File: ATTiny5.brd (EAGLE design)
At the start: 30 x 15 mm, 20 parts, among them Q1 BSP100, U1 SPX5205M5-L-3-3, U2 ATTINY5-TSHR, X1 DIODES, X2 INPUT

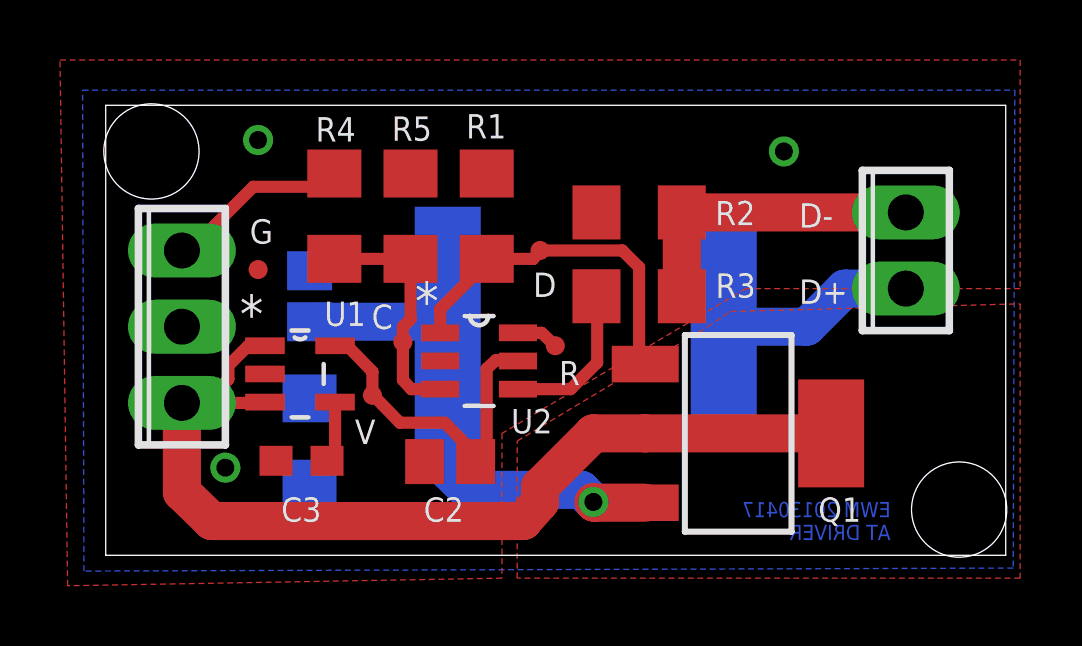
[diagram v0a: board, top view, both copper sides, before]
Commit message: Updated Board
Updated Board with Optional current limiting transistor and properly
sized and connected output cap.
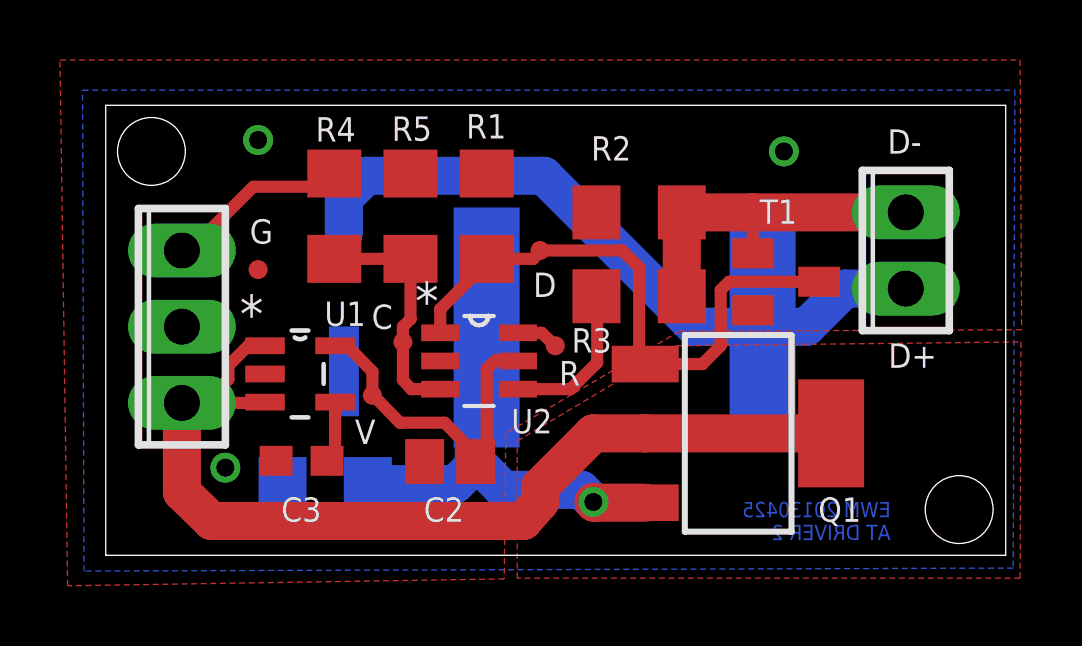
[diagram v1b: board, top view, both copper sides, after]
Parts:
- added T1: BC846, transistor:SOT23
- C1: value .1u -> 100u; device resistor:C0805 -> Personal:CDE-AVE-X
- moved D1 1.53 mm to (7.32, 2.37), turned to 0 degrees
- moved L1 1.30 mm to (17.3, 7.59)
- moved C1 1.16 mm to (7.94, 8.43)
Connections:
- net D-: now also T1.1
- net GND: now also C1.C-, T1.2; no longer C1.2
- net L+: no longer C1.1
- net MOSFET: now also T1.3
- net N$3: now also C1.C+
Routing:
- net N$3: track 6.59 -> 22.8 mm
- net MOSFET: track 11.9 -> 19.9 mm
- net D-: track 10.3 -> 11.6 mm
- net L+: track 16.5 -> 15.2 mm
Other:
- board text added: "EWM 20130425 AT DRIVER 2"
- board text removed: "EWM 20130417 AT DRIVER"
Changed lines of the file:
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@@
 <wire x1="30" y1="15" x2="0" y2="15" width="0.0254" layer="20"/>
 <wire x1="0" y1="15" x2="0" y2="0" width="0.0254" layer="20"/>
-<text x="23.114" y="8.382" size="0.8128" layer="25">D+</text>
-<text x="23.114" y="10.922" size="0.8128" layer="25">D-</text>
-<hole x="1.524" y="13.462" drill="3.175"/>
-<hole x="28.448" y="1.524" drill="3.175"/>
-<text x="26.162" y="0.508" size="0.508" layer="16" font="vector" ratio="20" rot="MR0">EWM 20130417
-AT DRIVER</text>
+<text x="26.0858" y="6.2484" size="0.8128" layer="25">D+</text>
+<text x="26.0604" y="13.3858" size="0.8128" layer="25">D-</text>
+<hole x="1.524" y="13.462" drill="2.2606"/>
+<hole x="28.448" y="1.524" drill="2.2606"/>
+<text x="26.162" y="0.508" size="0.508" layer="16" font="vector" ratio="20" rot="MR0">EWM 20130425
+AT DRIVER 2</text>
 <text x="14.2494" y="8.6106" size="0.8128" layer="25">D</text>
 <text x="8.8646" y="7.5438" size="0.8128" layer="25">C</text>
@@
 </element>
 <element name="R2" library="resistor" package="R1206" value="1" x="17.78" y="11.43" smashed="yes">
-<attribute name="NAME" x="20.32" y="10.9982" size="0.8128" layer="25"/>
+<attribute name="NAME" x="16.1798" y="13.1572" size="0.8128" layer="25"/>
 <attribute name="VALUE" x="16.383" y="9.017" size="1.27" layer="27"/>
 </element>
@@
 </element>
 <element name="R3" library="resistor" package="R1206" value="10k" x="17.78" y="8.636" smashed="yes" rot="R180">
-<attribute name="NAME" x="21.6662" y="9.398" size="0.8128" layer="25" rot="R180"/>
+<attribute name="NAME" x="16.8656" y="7.5692" size="0.8128" layer="25" rot="R180"/>
 <attribute name="VALUE" x="19.177" y="11.049" size="1.27" layer="27" rot="R180"/>
 </element>
-<element name="L1" library="Personal" package="SRN8040" value="SRN8040" x="16.002" y="7.62" smashed="yes" rot="MR180"/>
-<element name="D1" library="Personal" package="D1206" value="CD1206-B260" x="6.796" y="3.81" smashed="yes" rot="MR270">
-<attribute name="NAME" x="3.875" y="1.651" size="0.8128" layer="26" rot="MR180"/>
+<element name="L1" library="Personal" package="SRN8040" value="SRN8040" x="17.2974" y="7.5946" smashed="yes" rot="MR180"/>
+<element name="D1" library="Personal" package="D1206" value="CD1206-B260" x="7.3152" y="2.3734" smashed="yes" rot="MR0">
+<attribute name="NAME" x="5.1562" y="5.2944" size="0.8128" layer="26" rot="MR270"/>
 </element>
 <element name="R4" library="resistor" package="R1206" value="900" x="7.62" y="11.303" smashed="yes" rot="R90">
@@
 <attribute name="VALUE" x="12.573" y="9.906" size="1.27" layer="27" rot="R90"/>
 </element>
-<element name="C1" library="resistor" package="C0805" value=".1u" x="6.796" y="8.636" smashed="yes" rot="MR90">
-<attribute name="NAME" x="7.685" y="5.334" size="0.8128" layer="26" rot="MR0"/>
-<attribute name="VALUE" x="4.51" y="7.747" size="1.27" layer="28" rot="MR90"/>
+<element name="C1" library="Personal" package="CDE-AVE-X" value="100u" x="7.939" y="8.4328" smashed="yes" rot="MR90">
+<attribute name="NAME" x="8.828" y="5.1308" size="0.8128" layer="26" rot="MR0"/>
+<attribute name="VALUE" x="5.653" y="7.5438" size="1.27" layer="28" rot="MR90"/>
 </element>
 <element name="R1" library="resistor" package="R1206" value="10k" x="12.7" y="11.303" smashed="yes" rot="R270">
@@
 </element>
 <element name="RESET" library="Personal" package="TPI_PAD" value="TPI" x="14.986" y="6.985"/>
+<element name="T1" library="transistor" package="SOT23" value="BC846" x="22.6822" y="9.1186" smashed="yes" rot="R270">
+<attribute name="NAME" x="21.7932" y="11.049" size="0.8128" layer="25"/>
+<attribute name="VALUE" x="19.5072" y="11.0236" size="1.27" layer="27" rot="R270"/>
+</element>
 </elements>
 <signals>
@@
 <contactref element="R5" pad="2"/>
 <contactref element="D1" pad="2"/>
-<contactref element="C1" pad="2"/>
+<contactref element="C1" pad="C-"/>
 <contactref element="R1" pad="1"/>
 <contactref element="X2" pad="2"/>
@@
 <vertex x="-1.524" y="16.51"/>
 <vertex x="30.48" y="16.51"/>
-<vertex x="30.48" y="8.89"/>
-<vertex x="21.336" y="8.89"/>
-<vertex x="13.208" y="4.064"/>
-<vertex x="13.208" y="-0.762"/>
+<vertex x="30.5308" y="7.5184"/>
+<vertex x="19.1262" y="7.4676"/>
+<vertex x="13.335" y="4.064"/>
+<vertex x="13.2842" y="-0.7874"/>
 <vertex x="-1.27" y="-1.016"/>
 </polygon>
@@
 <contactref element="GND" pad="P$1"/>
 <contactref element="C3" pad="2"/>
+<contactref element="T1" pad="2"/>
 </signal>
 <signal name="+14V">
@@
 <polygon width="0.254" layer="1">
 <vertex x="13.716" y="3.81"/>
-<vertex x="20.066" y="7.62"/>
-<vertex x="20.828" y="8.128"/>
-<vertex x="30.48" y="8.382"/>
+<vertex x="18.161" y="6.4516"/>
+<vertex x="19.0246" y="6.985"/>
+<vertex x="30.5054" y="7.112"/>
 <vertex x="30.48" y="-0.762"/>
 <vertex x="13.716" y="-0.762"/>
@@
 <contactref element="R2" pad="2"/>
 <contactref element="R3" pad="1"/>
-<wire x1="26.67" y1="11.43" x2="19.202" y2="11.43" width="1.27" layer="1"/>
+<wire x1="26.67" y1="11.43" x2="21.5646" y2="11.43" width="1.27" layer="1"/>
+<wire x1="21.5646" y1="11.43" x2="19.202" y2="11.43" width="1.27" layer="1"/>
 <wire x1="19.202" y1="11.43" x2="19.202" y2="8.636" width="1.27" layer="1"/>
+<contactref element="T1" pad="1"/>
+<wire x1="21.5822" y1="10.0686" x2="21.5646" y2="10.0686" width="0.4064" layer="1"/>
+<wire x1="21.5646" y1="10.0686" x2="21.5646" y2="11.43" width="0.4064" layer="1"/>
 </signal>
 <signal name="MEASURE">
@@
 <wire x1="17.78" y1="9.6012" x2="17.78" y2="6.578" width="0.4064" layer="1"/>
 <wire x1="17.78" y1="6.578" x2="17.983" y2="6.375" width="0.4064" layer="1"/>
+<contactref element="T1" pad="3"/>
+<wire x1="23.7822" y1="9.1186" x2="20.7772" y2="9.1186" width="0.4064" layer="1"/>
+<wire x1="20.7772" y1="9.1186" x2="20.4978" y2="8.8392" width="0.4064" layer="1"/>
+<wire x1="20.4978" y1="8.8392" x2="20.4978" y2="6.985" width="0.4064" layer="1"/>
+<wire x1="20.4978" y1="6.985" x2="19.8882" y2="6.3754" width="0.4064" layer="1"/>
+<wire x1="19.8882" y1="6.3754" x2="17.9834" y2="6.3754" width="0.4064" layer="1"/>
+<wire x1="17.9834" y1="6.3754" x2="17.983" y2="6.375" width="0.4064" layer="1"/>
 </signal>
 <signal name="BLINK">
@@
 <contactref element="D1" pad="1"/>
 <contactref element="Q1" pad="3"/>
-<contactref element="C1" pad="1"/>
 <contactref element="L1" pad="P$1"/>
 <via x="16.256" y="1.778" extent="1-16" drill="0.6"/>
@@
 <wire x1="17.983" y1="1.753" x2="16.281" y2="1.753" width="1.27" layer="1"/>
 <wire x1="16.281" y1="1.753" x2="16.256" y2="1.778" width="1.27" layer="1"/>
-<wire x1="6.796" y1="7.786" x2="11.236" y2="7.786" width="1.27" layer="16"/>
-<wire x1="11.236" y1="7.786" x2="11.402" y2="7.62" width="1.27" layer="16"/>
-<wire x1="15.852" y1="2.182" x2="12.042" y2="2.182" width="1.27" layer="16"/>
-<wire x1="12.042" y1="2.182" x2="11.43" y2="2.794" width="1.27" layer="16"/>
-<wire x1="11.43" y1="2.794" x2="11.43" y2="7.592" width="1.27" layer="16"/>
-<wire x1="11.43" y1="7.592" x2="11.402" y2="7.62" width="1.27" layer="16"/>
-<wire x1="6.796" y1="7.786" x2="6.796" y2="5.232" width="0" layer="19" extent="16-16"/>
+<wire x1="15.852" y1="2.182" x2="13.2612" y2="2.182" width="1.27" layer="16"/>
+<wire x1="13.2612" y1="2.182" x2="12.372934375" y2="3.0929875" width="1.27" layer="16"/>
+<wire x1="12.372934375" y1="3.0929875" x2="12.2682" y2="3.2004" width="1.27" layer="16"/>
+<wire x1="12.6974" y1="7.5946" x2="12.2682" y2="7.5946" width="1.27" layer="16"/>
+<wire x1="12.2682" y1="7.5946" x2="12.2682" y2="6.1976" width="1.27" layer="16"/>
+<wire x1="12.2682" y1="6.1976" x2="12.2682" y2="3.2004" width="1.27" layer="16"/>
+<wire x1="12.2174" y1="6.2484" x2="12.2682" y2="6.1976" width="1.27" layer="16"/>
+<wire x1="8.7372" y1="2.3734" x2="11.653346875" y2="2.3734" width="1.27" layer="16"/>
+<wire x1="11.653346875" y1="2.3734" x2="12.372934375" y2="3.0929875" width="1.27" layer="16"/>
 </signal>
 <signal name="N$3">
@@
 <wire x1="26.67" y1="8.89" x2="24.638" y2="8.89" width="1.27" layer="16"/>
 <wire x1="24.638" y1="8.89" x2="23.368" y2="7.62" width="1.27" layer="16"/>
-<wire x1="23.368" y1="7.62" x2="20.602" y2="7.62" width="1.27" layer="16"/>
+<wire x1="23.368" y1="7.62" x2="21.8974" y2="7.5946" width="1.27" layer="16"/>
+<contactref element="C1" pad="C+"/>
+<wire x1="7.939" y1="10.7328" x2="7.939" y2="11.9014" width="1.27" layer="16"/>
+<wire x1="7.939" y1="11.9014" x2="8.6868" y2="12.6492" width="1.27" layer="16"/>
+<wire x1="8.6868" y1="12.6492" x2="14.605" y2="12.6492" width="1.27" layer="16"/>
+<wire x1="14.605" y1="12.6492" x2="19.6342" y2="7.62" width="1.27" layer="16"/>
+<wire x1="19.6342" y1="7.62" x2="21.872" y2="7.62" width="1.27" layer="16"/>
+<wire x1="21.872" y1="7.62" x2="21.8974" y2="7.5946" width="1.27" layer="16"/>
 </signal>
 <signal name="N$1">
